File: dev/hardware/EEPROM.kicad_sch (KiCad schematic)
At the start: 6 parts, among them U401 24LC256, U402 24LC256

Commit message: Thicc-traced VGA sig test - REVERT HERE
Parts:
- renumbered C1 to C?, R301 to R?
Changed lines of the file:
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@@
   (symbol (lib_id "Device:R") (at 187.96 91.44 180) (unit 1)
     (in_bom yes) (on_board yes) (dnp no) (fields_autoplaced)
-    (property "Reference" "R301" (at 190.5 90.17 0)
+    (property "Reference" "R?" (at 190.5 90.17 0)
       (effects (font (size 1.27 1.27)) (justify right))
     )
@@
       (project "jcap"
         (path "/7fc25e9e-3600-419b-89ef-b962e4e374c1/f5a50cf1-3d87-469f-beb1-b0b9cfae00ce"
-          (reference "R301") (unit 1)
+          (reference "R?") (unit 1)
         )
         (path "/7fc25e9e-3600-419b-89ef-b962e4e374c1/fef6ede6-5843-4140-8b23-7dcea4adc604"
@@
   (symbol (lib_id "Device:C") (at 95.25 87.63 0) (mirror x) (unit 1)
     (in_bom yes) (on_board yes) (dnp no) (fields_autoplaced)
-    (property "Reference" "C1" (at 91.44 86.36 0)
+    (property "Reference" "C?" (at 91.44 86.36 0)
       (effects (font (size 1.27 1.27)) (justify right))
     )
@@
       (project "jcap"
         (path "/7fc25e9e-3600-419b-89ef-b962e4e374c1"
-          (reference "C1") (unit 1)
-        )
-        (path "/7fc25e9e-3600-419b-89ef-b962e4e374c1/203ea849-2dbb-4e64-89c6-7fa05a05e11f"
-          (reference "C204") (unit 1)
+          (reference "C?") (unit 1)
+        )
+        (path "/7fc25e9e-3600-419b-89ef-b962e4e374c1/203ea849-2dbb-4e64-89c6-7fa05a05e11f"
+          (reference "C?") (unit 1)
         )
         (path "/7fc25e9e-3600-419b-89ef-b962e4e374c1/fef6ede6-5843-4140-8b23-7dcea4adc604"
@@
   (symbol (lib_id "Device:R") (at 119.38 91.44 180) (unit 1)
     (in_bom yes) (on_board yes) (dnp no) (fields_autoplaced)
-    (property "Reference" "R301" (at 121.92 90.17 0)
+    (property "Reference" "R?" (at 121.92 90.17 0)
       (effects (font (size 1.27 1.27)) (justify right))
     )
@@
       (project "jcap"
         (path "/7fc25e9e-3600-419b-89ef-b962e4e374c1/f5a50cf1-3d87-469f-beb1-b0b9cfae00ce"
-          (reference "R301") (unit 1)
+          (reference "R?") (unit 1)
         )
         (path "/7fc25e9e-3600-419b-89ef-b962e4e374c1/fef6ede6-5843-4140-8b23-7dcea4adc604"
@@
   (symbol (lib_id "power:+3.3V") (at 95.25 83.82 0) (mirror y) (unit 1)
     (in_bom yes) (on_board yes) (dnp no) (fields_autoplaced)
-    (property "Reference" "#PWR0213" (at 95.25 87.63 0)
+    (property "Reference" "#PWR?" (at 95.25 87.63 0)
       (effects (font (size 1.27 1.27)) hide)
     )
@@
       (project "jcap"
         (path "/7fc25e9e-3600-419b-89ef-b962e4e374c1/203ea849-2dbb-4e64-89c6-7fa05a05e11f"
-          (reference "#PWR0213") (unit 1)
+          (reference "#PWR?") (unit 1)
         )
         (path "/7fc25e9e-3600-419b-89ef-b962e4e374c1/fef6ede6-5843-4140-8b23-7dcea4adc604"
@@
   (symbol (lib_id "power:GND") (at 102.87 111.76 0) (unit 1)
     (in_bom yes) (on_board yes) (dnp no) (fields_autoplaced)
-    (property "Reference" "#PWR0402" (at 102.87 118.11 0)
+    (property "Reference" "#PWR0403" (at 102.87 118.11 0)
       (effects (font (size 1.27 1.27)) hide)
     )
@@
       (project "jcap"
         (path "/7fc25e9e-3600-419b-89ef-b962e4e374c1/fef6ede6-5843-4140-8b23-7dcea4adc604"
-          (reference "#PWR0402") (unit 1)
+          (reference "#PWR0403") (unit 1)
         )
       )
@@
   (symbol (lib_id "power:GND") (at 163.83 91.44 0) (mirror y) (unit 1)
     (in_bom yes) (on_board yes) (dnp no)
-    (property "Reference" "#PWR0215" (at 163.83 97.79 0)
+    (property "Reference" "#PWR?" (at 163.83 97.79 0)
       (effects (font (size 1.27 1.27)) hide)
     )
@@
       (project "jcap"
         (path "/7fc25e9e-3600-419b-89ef-b962e4e374c1/203ea849-2dbb-4e64-89c6-7fa05a05e11f"
-          (reference "#PWR0215") (unit 1)
-        )
-        (path "/7fc25e9e-3600-419b-89ef-b962e4e374c1/fef6ede6-5843-4140-8b23-7dcea4adc604"
-          (reference "#PWR0406") (unit 1)
+          (reference "#PWR?") (unit 1)
+        )
+        (path "/7fc25e9e-3600-419b-89ef-b962e4e374c1/fef6ede6-5843-4140-8b23-7dcea4adc604"
+          (reference "#PWR0405") (unit 1)
         )
       )
@@
   (symbol (lib_id "power:+3.3V") (at 163.83 83.82 0) (mirror y) (unit 1)
     (in_bom yes) (on_board yes) (dnp no) (fields_autoplaced)
-    (property "Reference" "#PWR0213" (at 163.83 87.63 0)
+    (property "Reference" "#PWR?" (at 163.83 87.63 0)
       (effects (font (size 1.27 1.27)) hide)
     )
@@
       (project "jcap"
         (path "/7fc25e9e-3600-419b-89ef-b962e4e374c1/203ea849-2dbb-4e64-89c6-7fa05a05e11f"
-          (reference "#PWR0213") (unit 1)
-        )
-        (path "/7fc25e9e-3600-419b-89ef-b962e4e374c1/fef6ede6-5843-4140-8b23-7dcea4adc604"
-          (reference "#PWR0405") (unit 1)
+          (reference "#PWR?") (unit 1)
+        )
+        (path "/7fc25e9e-3600-419b-89ef-b962e4e374c1/fef6ede6-5843-4140-8b23-7dcea4adc604"
+          (reference "#PWR0404") (unit 1)
         )
       )
@@
   (symbol (lib_id "Device:C") (at 163.83 87.63 0) (mirror x) (unit 1)
     (in_bom yes) (on_board yes) (dnp no) (fields_autoplaced)
-    (property "Reference" "C1" (at 160.02 86.36 0)
+    (property "Reference" "C?" (at 160.02 86.36 0)
       (effects (font (size 1.27 1.27)) (justify right))
     )
@@
       (project "jcap"
         (path "/7fc25e9e-3600-419b-89ef-b962e4e374c1"
-          (reference "C1") (unit 1)
-        )
-        (path "/7fc25e9e-3600-419b-89ef-b962e4e374c1/203ea849-2dbb-4e64-89c6-7fa05a05e11f"
-          (reference "C204") (unit 1)
+          (reference "C?") (unit 1)
+        )
+        (path "/7fc25e9e-3600-419b-89ef-b962e4e374c1/203ea849-2dbb-4e64-89c6-7fa05a05e11f"
+          (reference "C?") (unit 1)
         )
         (path "/7fc25e9e-3600-419b-89ef-b962e4e374c1/fef6ede6-5843-4140-8b23-7dcea4adc604"
@@
   (symbol (lib_id "power:GND") (at 171.45 111.76 0) (unit 1)
     (in_bom yes) (on_board yes) (dnp no) (fields_autoplaced)
-    (property "Reference" "#PWR0403" (at 171.45 118.11 0)
+    (property "Reference" "#PWR0406" (at 171.45 118.11 0)
       (effects (font (size 1.27 1.27)) hide)
     )
@@
       (project "jcap"
         (path "/7fc25e9e-3600-419b-89ef-b962e4e374c1/fef6ede6-5843-4140-8b23-7dcea4adc604"
-          (reference "#PWR0403") (unit 1)
+          (reference "#PWR0406") (unit 1)
         )
       )
@@
   (symbol (lib_id "power:GND") (at 95.25 91.44 0) (mirror y) (unit 1)
     (in_bom yes) (on_board yes) (dnp no)
-    (property "Reference" "#PWR0215" (at 95.25 97.79 0)
+    (property "Reference" "#PWR?" (at 95.25 97.79 0)
       (effects (font (size 1.27 1.27)) hide)
     )
@@
       (project "jcap"
         (path "/7fc25e9e-3600-419b-89ef-b962e4e374c1/203ea849-2dbb-4e64-89c6-7fa05a05e11f"
-          (reference "#PWR0215") (unit 1)
-        )
-        (path "/7fc25e9e-3600-419b-89ef-b962e4e374c1/fef6ede6-5843-4140-8b23-7dcea4adc604"
-          (reference "#PWR0404") (unit 1)
-        )
-      )
+          (reference "#PWR?") (unit 1)
+        )
+        (path "/7fc25e9e-3600-419b-89ef-b962e4e374c1/fef6ede6-5843-4140-8b23-7dcea4adc604"
+          (reference "#PWR0402") (unit 1)
+        )
+      )

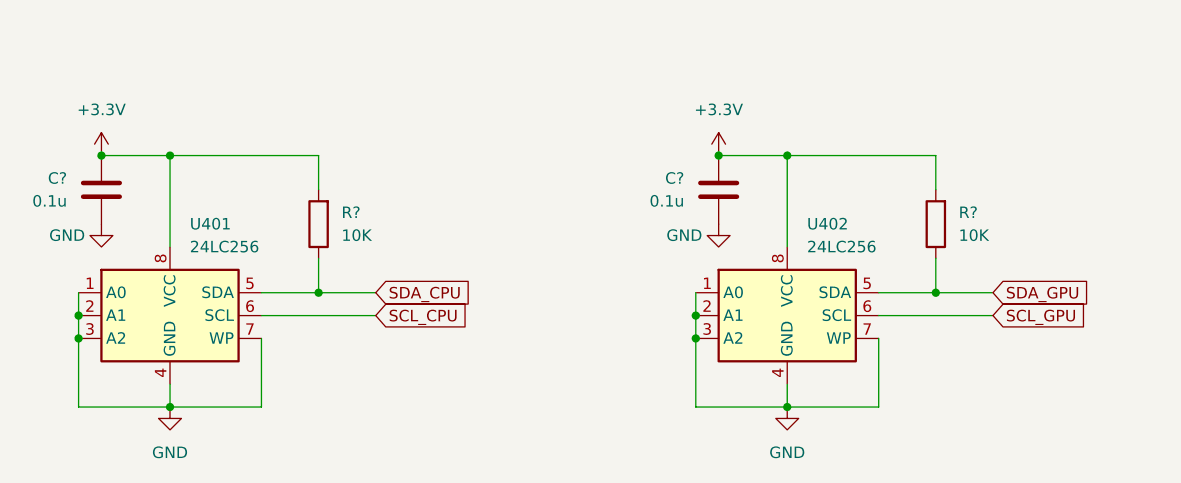
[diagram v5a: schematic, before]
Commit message: Implemented review changes - missing reverse polarity protection
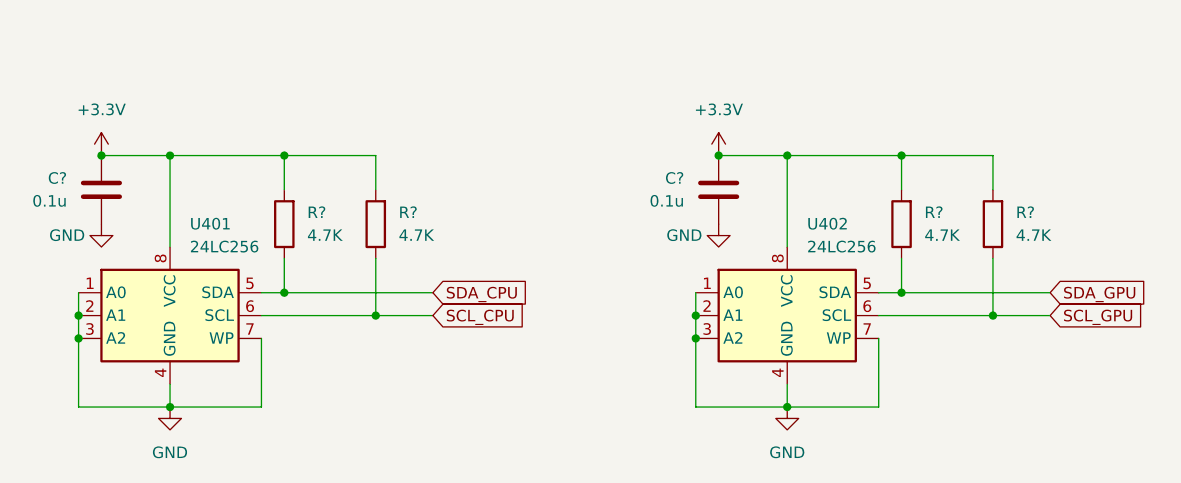
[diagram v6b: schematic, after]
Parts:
- added R? (x2): 4.7K, Resistor_THT:R_Axial_DIN0207_L6.3mm_D2.5mm_P10.16mm_Horizontal, symbol Device:R
- R? (x2): value 10K -> 4.7K
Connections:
- net +3.3V: now also R?.2, R?.2
- net SCL_CPU: now also R?.1
- net SCL_GPU: now also R?.1
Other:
- moved on the sheet: R?

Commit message: Finalized dev board administrivia
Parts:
- removed C? (x2): 0.1u, Capacitor_THT:C_Disc_D3.4mm_W2.1mm_P2.50mm, symbol Device:C
- removed R? (x3): 4.7K, Resistor_THT:R_Axial_DIN0207_L6.3mm_D2.5mm_P10.16mm_Horizontal, symbol Device:R
- added C? (x2): 0.1u, Capacitor_THT:C_Disc_D3.4mm_W2.1mm_P2.50mm, symbol Device:C
- added R? (x3): 4.7K, Resistor_THT:R_Axial_DIN0207_L6.3mm_D2.5mm_P10.16mm_Horizontal, symbol Device:R
- R?: Part (none) -> CF18JT4K70
- U401, U402: Part (none) -> 24LC256-I/P
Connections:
- net +3.3V: now also C?.2, C?.2, R?.2, R?.2, R?.2
- net GND: now also C?.1, C?.1
- net SCL_CPU: now also R?.1
- net SCL_GPU: now also R?.1
- net SDA_GPU: now also R?.1
